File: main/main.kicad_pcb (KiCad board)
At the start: 2 copper layers, 100 x 100 mm, 249 parts, among them J1 USB_B_Micro, J2 SWD, SW1 SW_SPST, SW2 SW_SPST, SW3 SW_SPST, SW4 SW_SPST, SW5 SW_SPST, SW6 SW_SPST, U1 LN6206P332MR-G, U2 STM32F401CBUx, Y1 Crystal

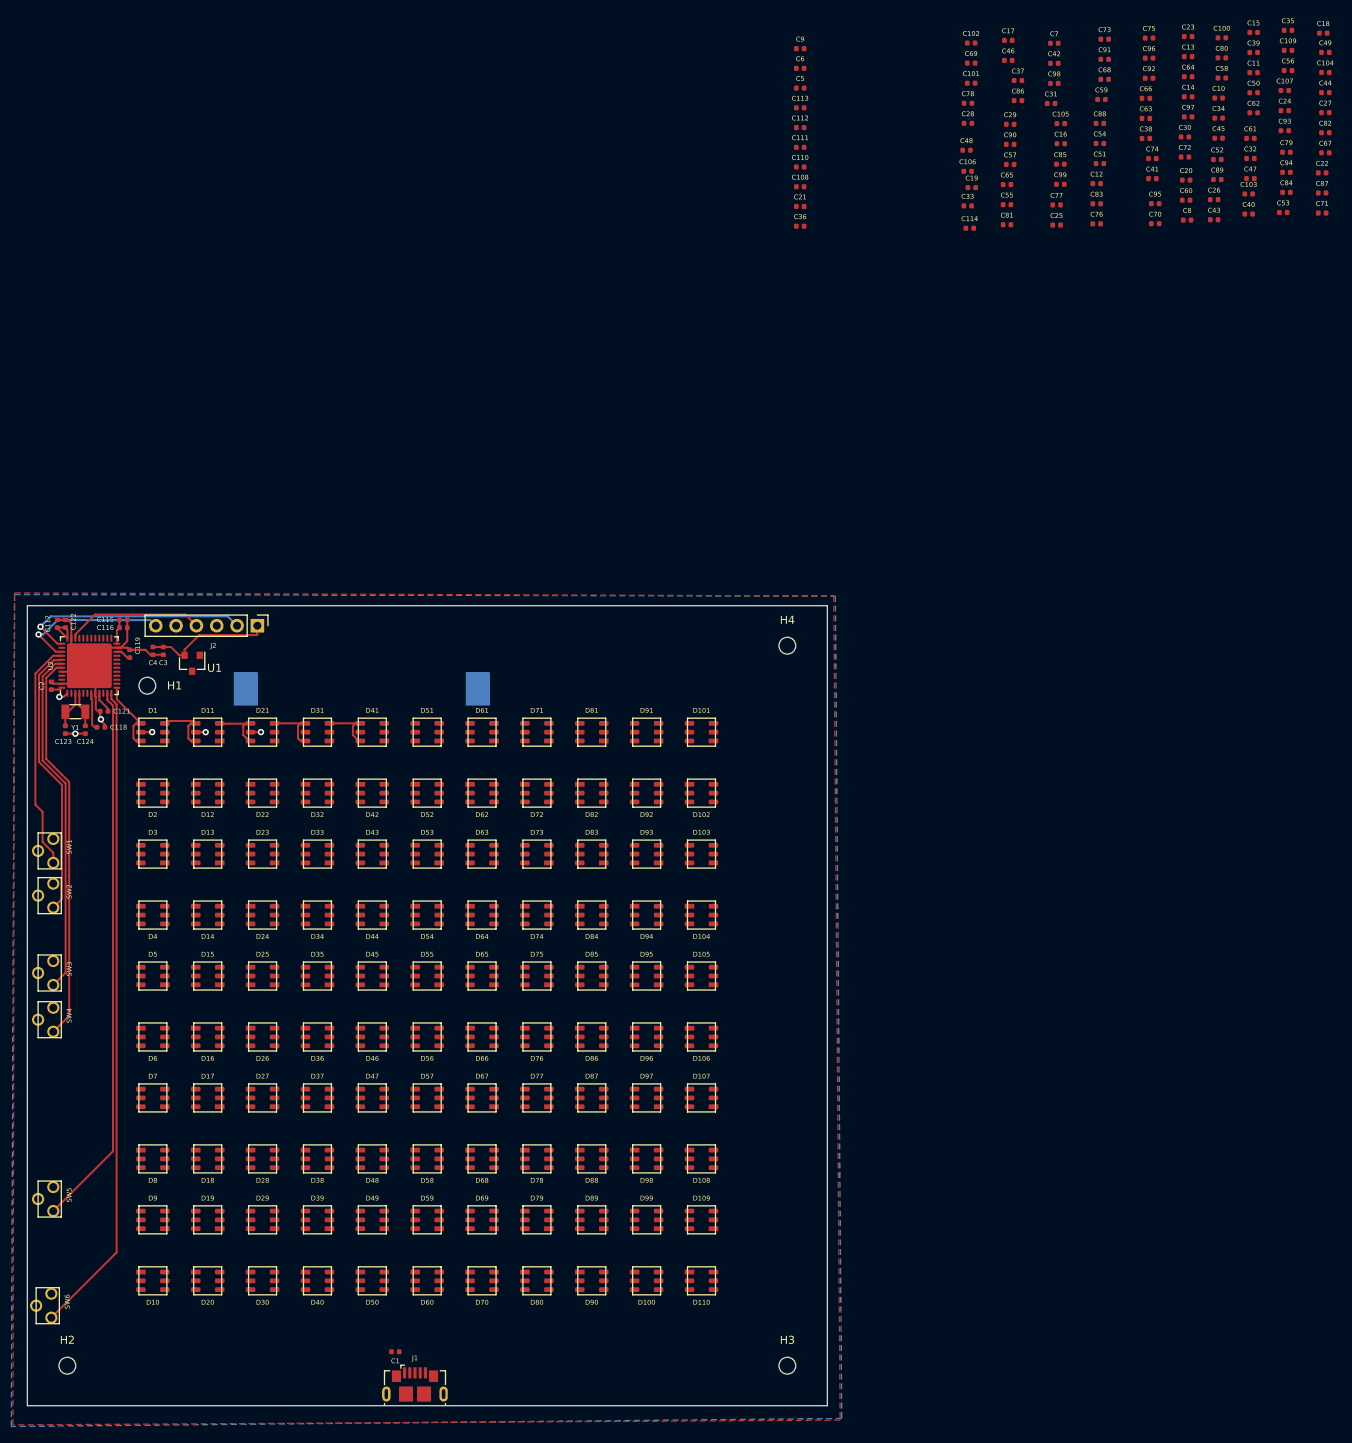
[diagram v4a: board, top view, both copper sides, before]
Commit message: most layout finished?  not super happy w/ star topology, but not lots of noise from this system, so probably just fine. now to add caps...
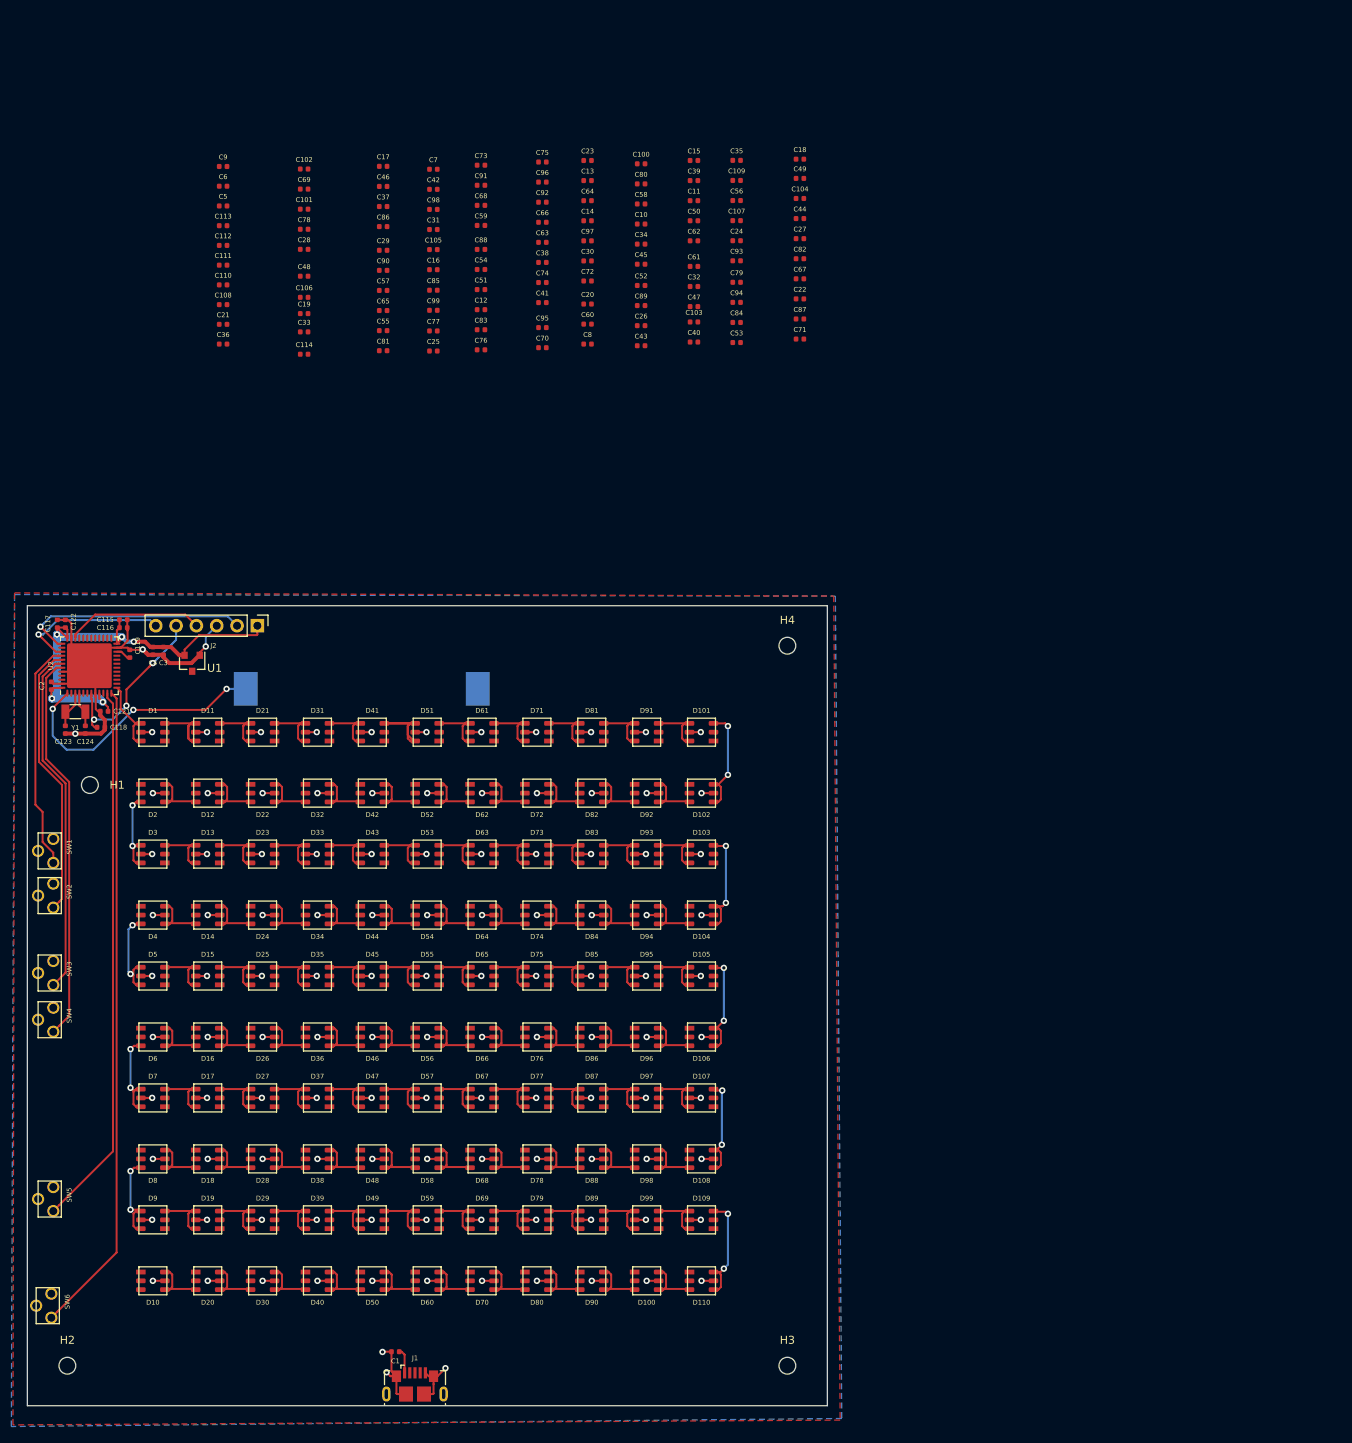
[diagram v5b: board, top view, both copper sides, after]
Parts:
- moved C19 84.9 mm to (34.6, -36.5)
- moved C101 84.9 mm to (34.6, -49.6)
- moved C102 84.9 mm to (34.6, -54.6)
- moved C69 84.9 mm to (34.6, -52.1)
- moved C114 84.7 mm to (34.6, -31.4)
- moved C28 84.5 mm to (34.6, -44.5)
- moved C78 84.5 mm to (34.6, -47.1)
- moved C106 84.4 mm to (34.6, -38.5)
- moved C33 84.4 mm to (34.6, -34.2)
- moved C48 84.3 mm to (34.6, -41.2)
- moved C37 80.9 mm to (44.5, -49.9)
- moved C86 80.9 mm to (44.5, -47.4)
- moved C105 80.0 mm to (50.8, -44.5)
- moved C16 80.0 mm to (50.8, -42.0)
- moved C29 79.9 mm to (44.5, -44.4)
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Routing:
- net GND: track 47.9 -> 232.3 mm, vias 5 -> 116
- net +BATT: track 1.19 -> 34.1 mm, vias 1 -> 3
- net +3V3: track 27.6 -> 58.2 mm, vias 0 -> 5
- net /mic/~RST: track 4.73 -> 22.1 mm, vias 0 -> 3
- net Net-(D41-Pad3): track 0.00 -> 14.8 mm
- net Net-(D109-Pad3): track 0.00 -> 14.1 mm, vias 0 -> 2
- net Net-(D103-Pad3): track 0.00 -> 14.1 mm, vias 0 -> 2
- net Net-(D101-Pad3): track 0.00 -> 13.4 mm, vias 0 -> 2
- net Net-(D105-Pad3): track 0.00 -> 13.3 mm, vias 0 -> 2
- net Net-(D107-Pad3): track 0.00 -> 13.0 mm, vias 0 -> 2
- net Net-(D4-Pad3): track 0.00 -> 11.6 mm, vias 0 -> 2
- net Net-(D6-Pad3): track 0.00 -> 11.4 mm, vias 0 -> 2
- net Net-(D8-Pad3): track 0.00 -> 11.3 mm, vias 0 -> 2
- net Net-(D2-Pad3): track 0.00 -> 11.0 mm, vias 0 -> 2
- net Net-(D104-Pad3): track 0.00 -> 7.60 mm
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
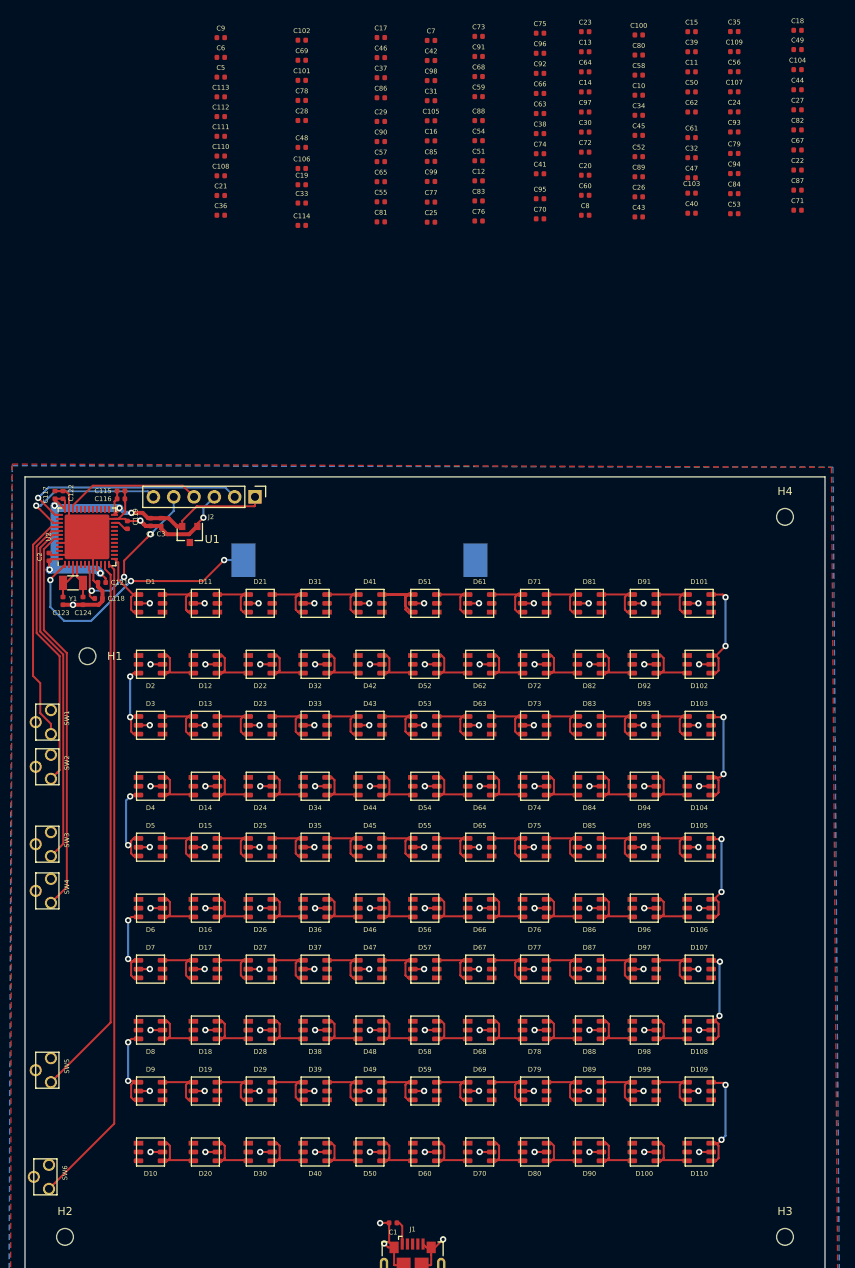
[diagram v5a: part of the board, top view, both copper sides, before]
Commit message: mostly done?  reviewing now.  Also need to fix/update USB connector
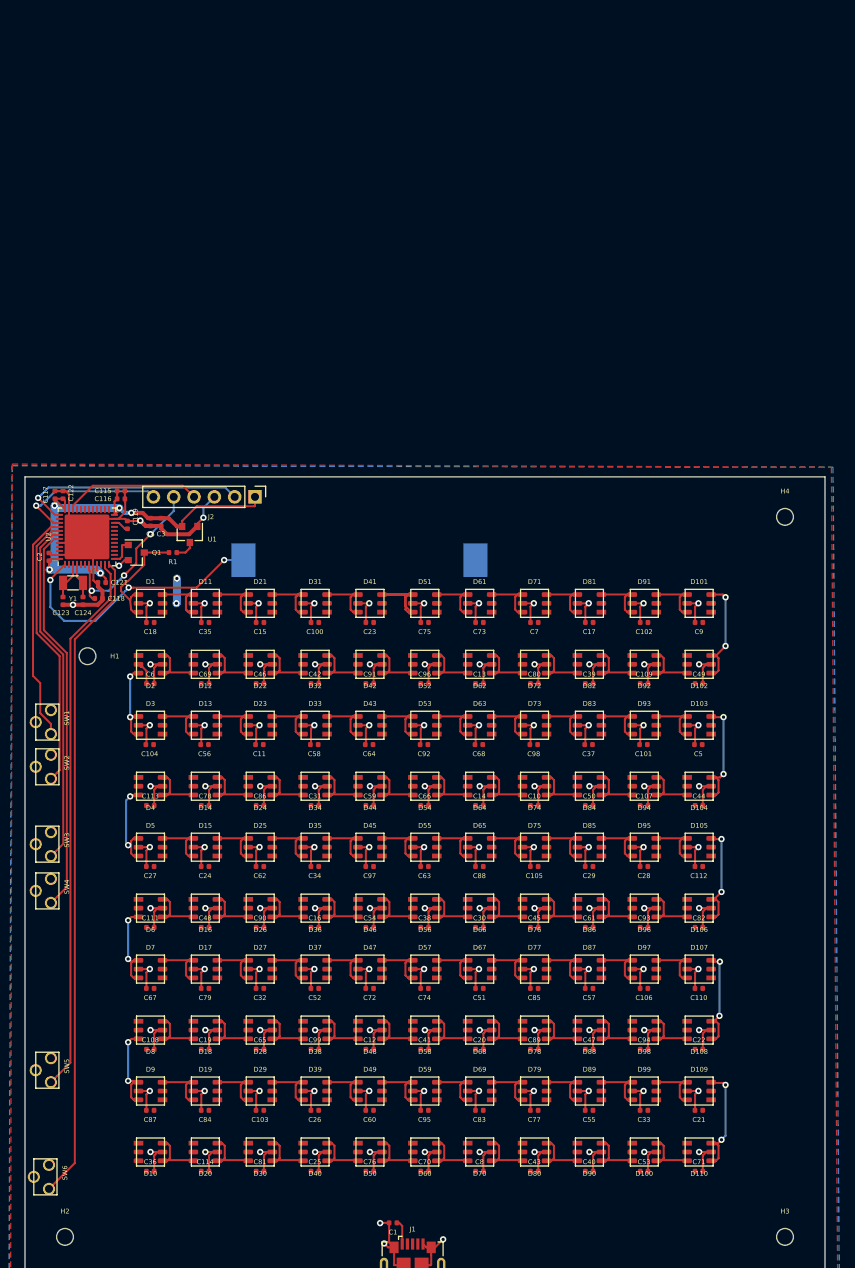
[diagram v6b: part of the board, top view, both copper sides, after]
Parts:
- added Q1: BSS138, Package_TO_SOT_SMD:SOT-23, F.Cu at (13.9, 9.46)
- added R1: 10K, Resistor_SMD:R_0402_1005Metric, F.Cu at (18.5, 9.46)
- moved C87 140.6 mm to (15.6, 79.2), turned to 180 degrees
- moved C67 132.4 mm to (15.6, 63.9), turned to 180 degrees
- moved C84 132.3 mm to (22.5, 79.2), turned to 180 degrees
- moved C21 129.0 mm to (84.2, 79.2), turned to 180 degrees
- moved C103 126.7 mm to (29.4, 79.2), turned to 180 degrees
- moved C27 124.5 mm to (15.6, 48.7), turned to 180 degrees
- moved C79 123.6 mm to (22.5, 63.9), turned to 180 degrees
- moved C33 121.2 mm to (77.4, 79.2), turned to 180 degrees
- moved C26 121.2 mm to (36.2, 79.2), turned to 180 degrees
- moved C71 120.8 mm to (84.2, 86.8)
- moved C40 120.4 mm to (70.5, 86.8)
- moved C8 120.2 mm to (56.8, 86.8)
- moved C53 120.2 mm to (77.4, 86.8)
- moved C43 120.0 mm to (63.7, 86.8)
- moved C110 120.0 mm to (84.2, 63.9), turned to 180 degrees
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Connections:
- D1 pad 4: /LEDs/DIN -> /~LED_DATA_OUT~_5V
- D1 pad 6: /LEDs/DIN -> /~LED_DATA_OUT~_5V
- U2 pad 13: /LEDs/DIN -> /mic/LED_DATA_OUT
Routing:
- net GND: track 232.3 -> 551.7 mm, vias 116 -> 117
- net /~LED_DATA_OUT~_5V: track 0.00 -> 14.5 mm
- net /LEDs/DIN: track 9.17 -> 0.00 mm
- net +5V: track 3.09 -> 11.7 mm, vias 0 -> 2
- net /mic/LED_DATA_OUT: track 0.00 -> 3.25 mm

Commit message: caps done, added FET for 5V logic to WS2813, reduced trace/space
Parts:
- J1: value USB_B_Micro -> USB_C_Receptacle; footprint Connector_USB:USB_Micro-B_GCT_USB3076-30-A -> william_usb:C168688
- moved C1 5.27 mm to (50.0, 89.8), turned to 90 degrees
- moved J1 4.59 mm to (50.0, 93.0)
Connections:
- net /mic/LED_DATA_OUT renamed /LED_DATA_OUT_3V3
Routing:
- net GND: track 551.7 -> 544.6 mm, vias 117 -> 120
- net +5V: track 11.7 -> 8.63 mm
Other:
- outline, holes or cut-outs redrawn

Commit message: v0.0.0 ready to send to fab
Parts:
- moved SW1 0.25 mm to (2.99, 29.2)
- moved SW2 0.25 mm to (2.99, 34.7)
- moved SW3 0.25 mm to (2.99, 44.4)
- moved SW4 0.25 mm to (2.99, 50.3)
- moved SW5 0.25 mm to (2.99, 72.7)
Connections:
- J1 pad A6: Net-(J1-PadA6) -> (no net)
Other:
- outline, holes or cut-outs redrawn
- board text added: "Battery = CR2032"
- board text added: "JLCPCB XXXXX"
- board text added: "USB Type C"
- board text added: "WORD CLOCK v0.0.0 batch 0 12/11/2019"
